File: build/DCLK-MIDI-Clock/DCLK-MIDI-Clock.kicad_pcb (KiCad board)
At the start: 2 copper layers, 125 x 213 mm, 75 parts, among them J1 MIDI OUT, J2 Jack-DC, J3 MIDI OUT, J5 Conn_02x04_Odd_Even, J6 Conn_02x04_Odd_Even, J7 SYNC 1 OUT, J8 SYNC 2 OUT, SW4 RotaryEncoder_Switch_MP, U2 CAP1206-x-SL, U3 74AHCT125

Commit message: pcb design update
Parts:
- added G***: LOGO, dclk:DCLK-Front-Panel_FMASK, B.Cu at (19.0, 153.0)
- moved G*** 68.6 mm to (19.0, 153.0)

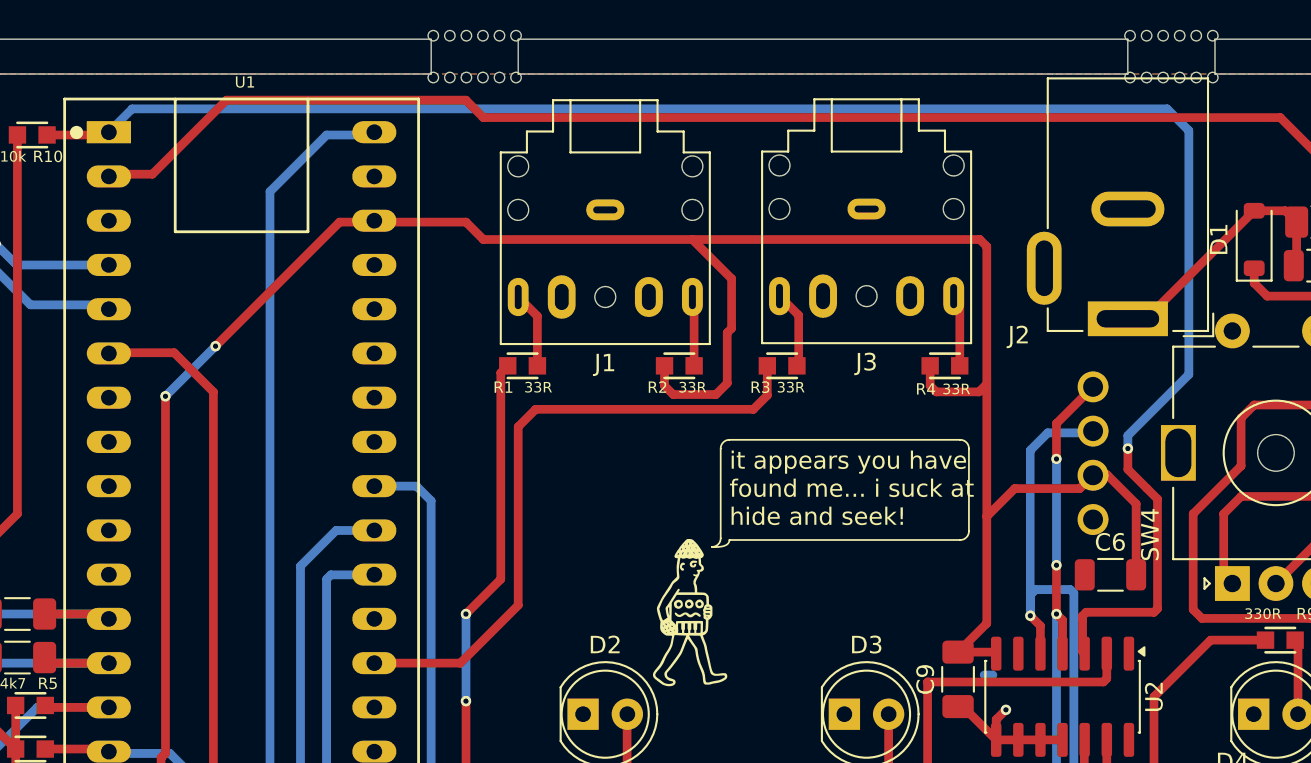
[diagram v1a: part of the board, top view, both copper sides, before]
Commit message: pcb update
-fixed oled positions
- fixed resistor inconsistencies
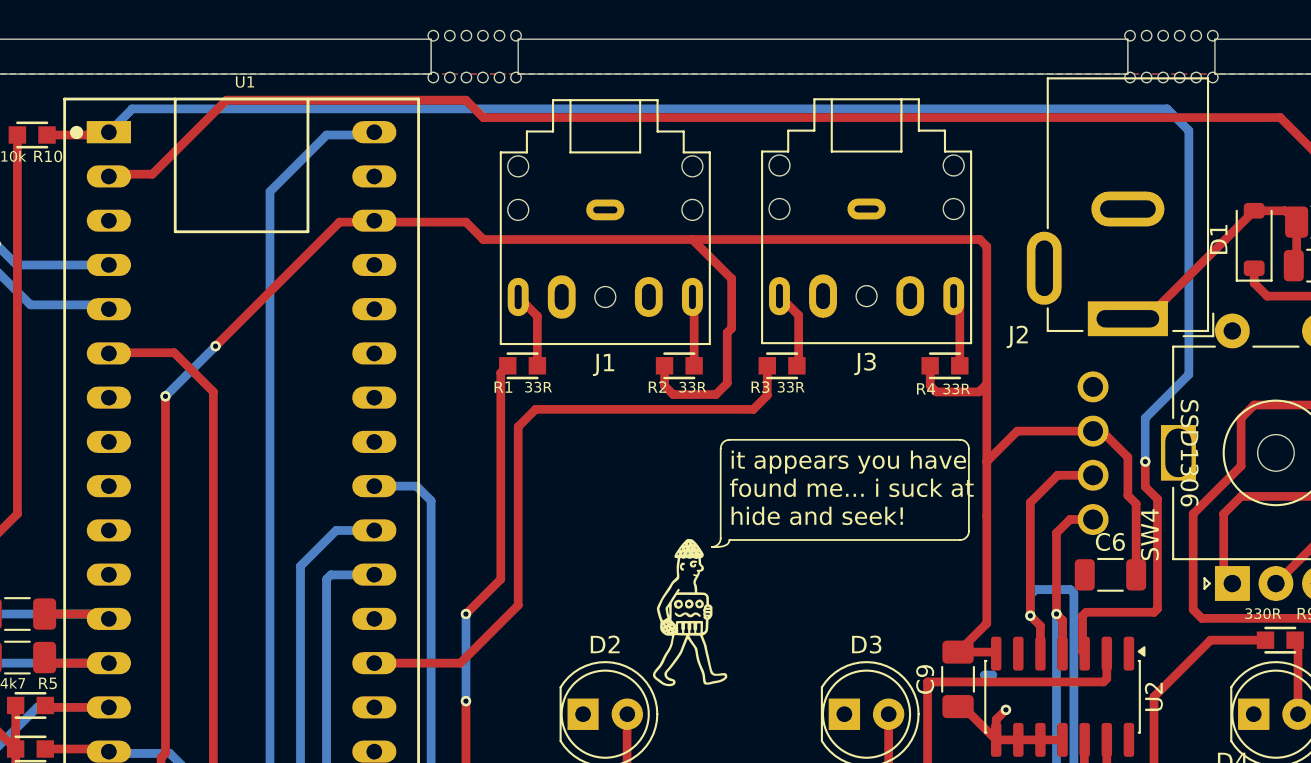
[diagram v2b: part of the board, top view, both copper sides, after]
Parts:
- SSD1306: moved to F.Cu
- moved SSD1306 2.00 mm to (109.5, 48.8), turned to -90 degrees
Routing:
- net SDA0: track 112.6 -> 105.7 mm, vias 5 -> 3
- net SCL0: track 136.1 -> 133.3 mm
- net 3V3: track 217.4 -> 219.6 mm
- net ISR: track 103.0 -> 102.2 mm

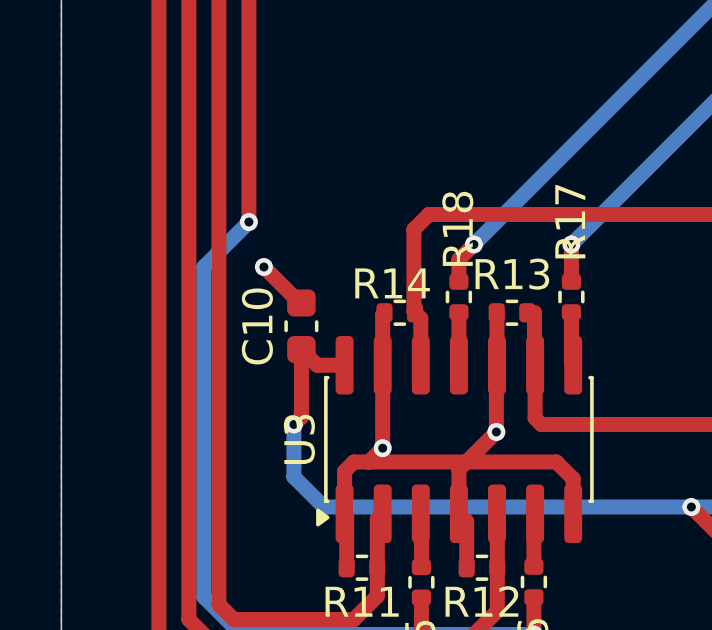
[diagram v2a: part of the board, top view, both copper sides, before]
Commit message: C10
updated to 1206
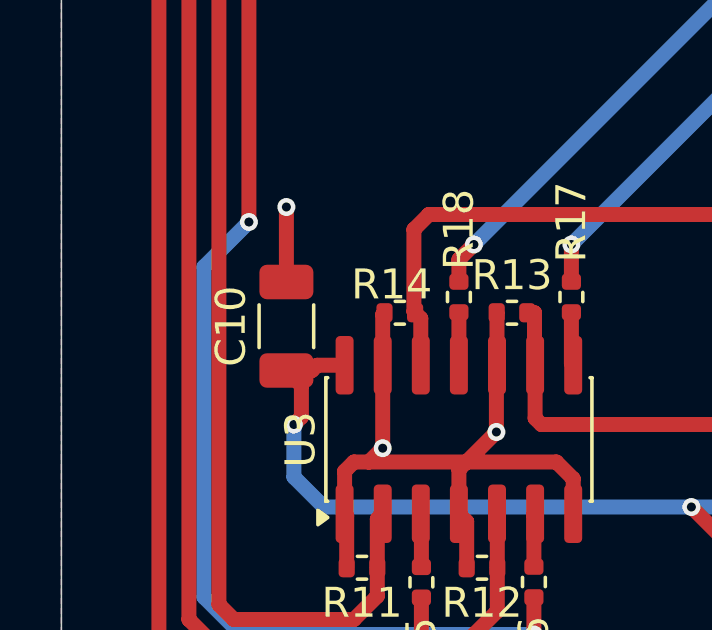
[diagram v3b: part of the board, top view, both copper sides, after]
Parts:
- C10: footprint Capacitor_SMD:C_0603_1608Metric -> Capacitor_SMD:C_1206_3216Metric
- moved C10 0.50 mm to (25.5, 66.0)
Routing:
- net GND: track 42.1 -> 42.9 mm
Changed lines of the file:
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@@
 		(embedded_fonts no)
 	)
-	(footprint "Capacitor_SMD:C_0603_1608Metric"
+	(footprint "Capacitor_SMD:C_1206_3216Metric"
 		(layer "F.Cu")
-		(at 26 65.975 90)
-		(descr "Capacitor SMD 0603 (1608 Metric), square (rectangular) end terminal, IPC-7351 nominal, (Body size source: IPC-SM-782 page 76, https://www.pcb-3d.com/wordpress/wp-content/uploads/ipc-sm-782a_amendment_1_and_2.pdf), generated with kicad-footprint-generator")
+		(at 25.5 65.975 90)
+		(descr "Capacitor SMD 1206 (3216 Metric), square (rectangular) end terminal, IPC-7351 nominal, (Body size source: IPC-SM-782 page 76, https://www.pcb-3d.com/wordpress/wp-content/uploads/ipc-sm-782a_amendment_1_and_2.pdf), generated with kicad-footprint-generator")
 		(tags "capacitor")
 		(property "Reference" "C10"
-			(at 0 -1.43 90)
+			(at 0 -1.85 90)
 			(layer "F.SilkS")
 			(effects
@@
 		)
 		(property "Value" "100nF"
-			(at 0 1.43 90)
+			(at 0 1.85 90)
 			(layer "F.Fab")
 			(effects
@@
 		(attr smd)
 		(fp_line
-			(start -0.140581 -0.51)
-			(end 0.140581 -0.51)
+			(start -0.711252 -0.91)
+			(end 0.711252 -0.91)
 			(stroke
 				(width 0.12)
@@
 		)
 		(fp_line
-			(start -0.140581 0.51)
-			(end 0.140581 0.51)
+			(start -0.711252 0.91)
+			(end 0.711252 0.91)
 			(stroke
 				(width 0.12)
@@
 			(layer "F.SilkS")
 		)
-		(fp_poly
-			(pts
-				(xy -1.48 -0.73) (xy 1.48 -0.73) (xy 1.48 0.73) (xy -1.48 0.73)
-			)
+		(fp_rect
+			(start -2.3 -1.15)
+			(end 2.3 1.15)
 			(stroke
 				(width 0.05)
@@
 			(layer "F.CrtYd")
 		)
-		(fp_poly
-			(pts
-				(xy -0.8 -0.4) (xy 0.8 -0.4) (xy 0.8 0.4) (xy -0.8 0.4)
-			)
+		(fp_rect
+			(start -1.6 -0.8)
+			(end 1.6 0.8)
 			(stroke
 				(width 0.1)
@@
 			(effects
 				(font
-					(size 0.4 0.4)
-					(thickness 0.06)
+					(size 0.8 0.8)
+					(thickness 0.12)
 				)
 			)
 		)
 		(pad "1" smd roundrect
-			(at -0.775 0 90)
-			(size 0.9 0.95)
+			(at -1.475 0 90)
+			(size 1.15 1.8)
 			(layers "F.Cu" "F.Mask" "F.Paste")
-			(roundrect_rratio 0.25)
+			(roundrect_rratio 0.217391)
 			(net 45 "Vcc")
 			(pintype "passive")
 		)
 		(pad "2" smd roundrect
-			(at 0.775 0 90)
-			(size 0.9 0.95)
+			(at 1.475 0 90)
+			(size 1.15 1.8)
 			(layers "F.Cu" "F.Mask" "F.Paste")
-			(roundrect_rratio 0.25)
+			(roundrect_rratio 0.217391)
 			(net 2 "GND")
 			(pintype "passive")
 		)
 		(embedded_fonts no)
-		(model "${KICAD9_3DMODEL_DIR}/Capacitor_SMD.3dshapes/C_0603_1608Metric.step"
+		(model "${KICAD9_3DMODEL_DIR}/Capacitor_SMD.3dshapes/C_1206_3216Metric.step"
 			(offset
 				(xyz 0 0 0)
@@
 			)
 		)
-		(property "Description" "10k, 1%, 1/16W, 0603"
+		(property "Description" "33R, 1%, 1/16W, 0603"
 			(at 0 0 0)
 			(layer "F.Fab")
@@
 			)
 		)
-		(property "Specifications" "10k, 1%, 1/10W, 0402"
+		(property "Specifications" "33R, 1%, 1/16W, 0603"
 			(at 0 0 0)
 			(unlocked yes)
@@
 			)
 		)
-		(property "Description" "10k, 1%, 1/16W, 0603"
+		(property "Description" "330R, 1%, 1/16W, 0603"
 			(at 0 0 0)
 			(layer "F.Fab")
@@
 			)
 		)
-		(property "Specifications" "10k, 1%, 1/10W, 0402"
+		(property "Specifications" "330R, 1%, 1/16W, 0603"
 			(at 0 0 0)
 			(unlocked yes)
@@
 			)
 		)
-		(property "Description" "10k, 1%, 1/16W, 0603"
+		(property "Description" "330R, 1%, 1/16W, 0603"
 			(at 0 0 0)
 			(layer "F.Fab")
@@
 			)
 		)
-		(property "Specifications" "10k, 1%, 1/10W, 0402"
+		(property "Specifications" "330R, 1%, 1/16W, 0603"
 			(at 0 0 0)
 			(unlocked yes)
@@
 			)
 		)
-		(property "Description" "10k, 1%, 1/16W, 0603"
+		(property "Description" "33R, 1%, 1/16W, 0603"
 			(at 0 0 0)
 			(layer "F.Fab")
@@
 			)
 		)
-		(property "Specifications" "10k, 1%, 1/10W, 0402"
+		(property "Specifications" "33R, 1%, 1/16W, 0603"
 			(at 0 0 0)
 			(unlocked yes)
@@
 			)
 		)
-		(property "Description" "10k, 1%, 1/16W, 0603"
+		(property "Description" "4k7, 1%, 1/16W, 0603"
 			(at 0 0 0)
 			(layer "F.Fab")
@@
 			)
 		)
-		(property "Specifications" "10k, 1%, 1/10W, 0402"
+		(property "Specifications" "4k7, 1%, 1/16W, 0603"
 			(at 0 0 0)
 			(unlocked yes)
@@
 			)
 		)
-		(property "Description" "10k, 1%, 1/16W, 0603"
+		(property "Description" "33R, 1%, 1/16W, 0603"
 			(at 0 0 0)
 			(layer "F.Fab")
@@
 			)
 		)
-		(property "Specifications" "10k, 1%, 1/10W, 0402"
+		(property "Specifications" "33R, 1%, 1/16W, 0603"
 			(at 0 0 0)
 			(unlocked yes)
@@
 			)
 		)
-		(property "Description" "10k, 1%, 1/16W, 0603"
+		(property "Description" "33R, 1%, 1/16W, 0603"
 			(at 0 0 0)
 			(layer "F.Fab")
@@
 			)
 		)
-		(property "Specifications" "10k, 1%, 1/10W, 0402"
+		(property "Specifications" "33R, 1%, 1/16W, 0603"
 			(at 0 0 0)
 			(unlocked yes)
@@
 			)
 		)
-		(property "Description" "10k, 1%, 1/16W, 0603"
+		(property "Description" "4k7, 1%, 1/16W, 0603"
 			(at 0 0 0)
 			(layer "F.Fab")
@@
 			)
 		)
-		(property "Specifications" "10k, 1%, 1/10W, 0402"
+		(property "Specifications" "4k7, 1%, 1/16W, 0603"
 			(at 0 0 0)
 			(unlocked yes)
@@
 			)
 		)
-		(property "Description" "10k, 1%, 1/16W, 0603"
+		(property "Description" "330R, 1%, 1/16W, 0603"
 			(at 0 0 0)
 			(layer "F.Fab")
@@
 			)
 		)
-		(property "Specifications" "10k, 1%, 1/10W, 0402"
+		(property "Specifications" "330R, 1%, 1/16W, 0603"
 			(at 0 0 0)
 			(unlocked yes)
@@
 	)
 	(segment
-		(start 25.95 65.2)
-		(end 24.75 64)
-		(width 0.5)
-		(layer "F.Cu")
-		(net 2)
-	)
-	(segment
 		(start 110.44 64.225)
 		(end 114.25 64.225)
@@
 	)
 	(segment
-		(start 28.71 70.04)
-		(end 28.25 70.5)
+		(start 25.5 62)
+		(end 25.5 64.5)
 		(width 0.5)
 		(layer "F.Cu")
@@
 	)
 	(segment
-		(start 26 65.2)
-		(end 25.95 65.2)
+		(start 28.71 70.04)
+		(end 28.25 70.5)
 		(width 0.5)
 		(layer "F.Cu")
@@
 	)
 	(via
-		(at 24.75 64)
+		(at 25.5 62)
 		(size 0.6)
 		(drill 0.3)
@@
 	)
 	(segment
+		(start 25.5 67.45)
+		(end 26.35 67.45)
+		(width 0.5)
+		(layer "F.Cu")
+		(net 45)
+	)
+	(segment
 		(start 40.25 82)
 		(end 40.25 73.25)
@@
 	)
 	(segment
-		(start 26.525 67.275)
-		(end 27.44 67.275)
+		(start 26 69)
+		(end 26 67.95)
 		(width 0.5)
 		(layer "F.Cu")
@@
 	)
 	(segment
-		(start 26 66.75)
-		(end 26 69)
+		(start 59.48 72.5)
+		(end 59.5 72.52)
 		(width 0.5)
 		(layer "F.Cu")
@@
 	)
 	(segment
-		(start 59.48 72.5)
-		(end 59.5 72.52)
+		(start 121 87.75)
+		(end 46 87.75)
 		(width 0.5)
 		(layer "F.Cu")
@@
 	)
 	(segment
-		(start 121 87.75)
-		(end 46 87.75)
+		(start 26 67.95)
+		(end 25.5 67.45)
+		(width 0.5)
+		(layer "F.Cu")
+		(net 45)
+	)
+	(segment
+		(start 26.525 67.275)
+		(end 27.44 67.275)
+		(width 0.5)
+		(layer "F.Cu")
+		(net 45)
+	)
+	(segment
+		(start 26.35 67.45)
+		(end 26.525 67.275)
 		(width 0.5)
 		(layer "F.Cu")
@@
 	)
 	(segment
-		(start 135.25 39.25)
-		(end 135.25 73.5)
+		(start 25.75 69.25)
+		(end 26 69)
 		(width 0.5)
 		(layer "F.Cu")
@@
 	)
 	(segment
-		(start 125.25 38)
-		(end 126 38.75)
+		(start 135.25 39.25)
+		(end 135.25 73.5)
 		(width 0.5)
 		(layer "F.Cu")
@@
 	)
 	(segment
-		(start 26 69)
-		(end 25.75 69.25)
+		(start 125.25 38)
+		(end 126 38.75)
 		(width 0.5)
 		(layer "F.Cu")
@@
 		(width 0.5)
 		(layer "F.Cu")
-		(net 45)
-	)
-	(segment
-		(start 26 66.75)
-		(end 26.525 67.275)
-		(width 0.5)
-		(layer "F.Cu")

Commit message: updated bom
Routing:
- net GND: vias 5 -> 6
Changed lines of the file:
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@@
+	)
+	(via
+		(at 117 54.5)
+		(size 0.6)
+		(drill 0.3)
+		(layers "F.Cu" "B.Cu")
+		(free yes)
+		(net 2)
 	)
 	(via

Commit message: Symbol Fields
C1/C6
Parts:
- C1, C6: value 100nF_0603_16V -> 100nF
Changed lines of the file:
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@@
 			)
 		)
-		(property "Value" "100nF_0603_16V"
+		(property "Value" "100nF"
 			(at 0 1.850001 0)
 			(layer "F.Fab")
@@
 			)
 		)
-		(property "Value" "100nF_0603_16V"
+		(property "Value" "100nF"
 			(at 0 1.85 0)
 			(layer "F.Fab")
